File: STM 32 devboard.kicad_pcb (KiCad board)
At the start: 2 copper layers, 20 x 50 mm, 29 parts, among them J1 Conn_01x10_Pin, J2 Conn_01x10_Pin, J3 USB_B_Micro, SW1 SW_SPDT, U1 AMS1117-3.3, U2 STM32F103C8T6, Y1 16MHz

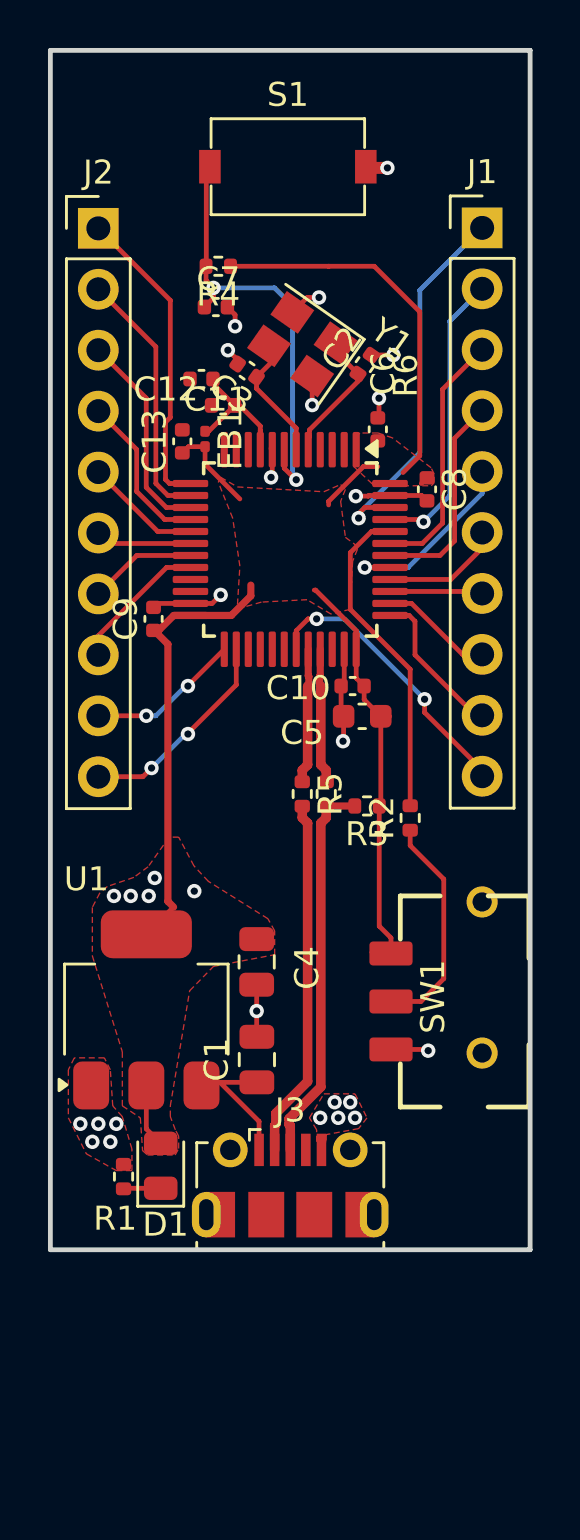
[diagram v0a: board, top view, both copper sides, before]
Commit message: Added USB-C port.
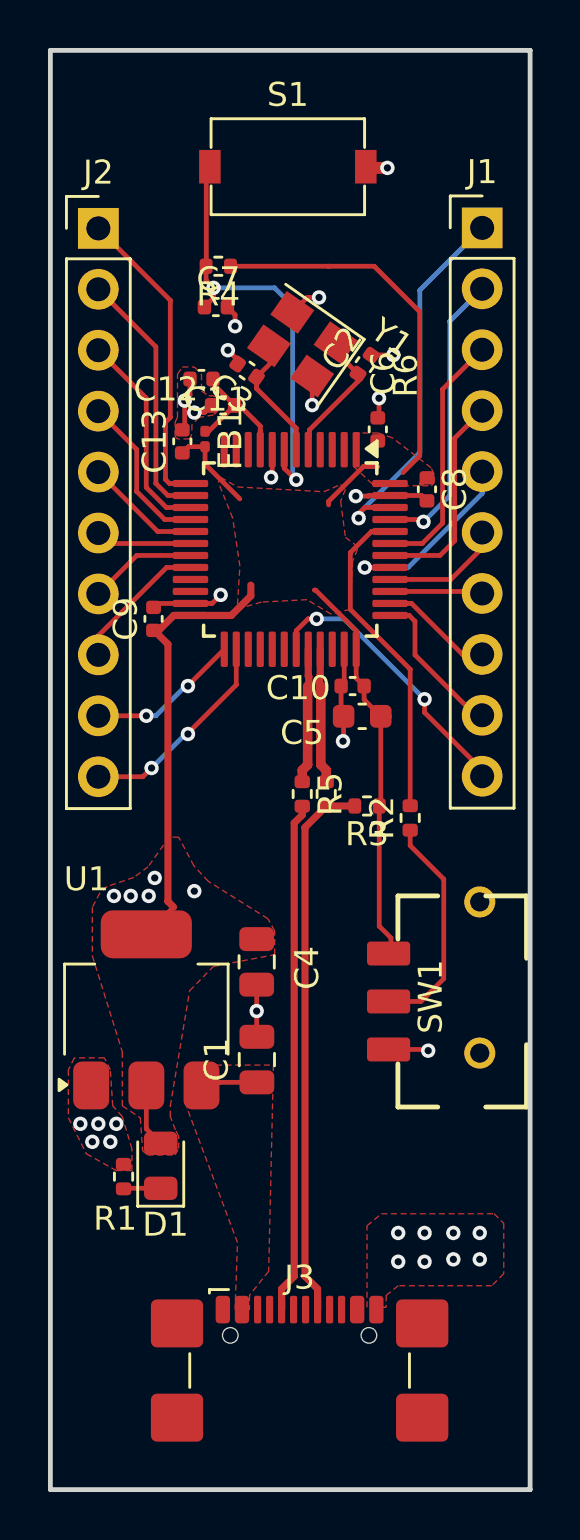
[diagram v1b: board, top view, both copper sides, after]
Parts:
- C1: value 22uF -> 22u
- C10, C6, C8, C9: value 100nF -> 100n
- C11: value 10nF -> 10n
- C12, C13: value 1uF -> 1u
- C2, C3: value 12pF -> 12p
- C5: value 10uF -> 10u
- J3: value USB_B_Micro -> USB_C_Receptacle; footprint Connector_USB:USB_Micro-B_Molex-105017-0001 -> Connector_USB:USB_C_Receptacle_GCT_USB4110
- moved J3 8.88 mm to (22.4, 68.2)
- moved SW1 0.10 mm to (27.4, 51.6)
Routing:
- net /USB_D+: track 16.2 -> 22.8 mm
- net /USB_D-: track 15.0 -> 21.3 mm
- net VBUS: track 6.50 -> 3.01 mm
- net GND: track 23.4 -> 25.9 mm, vias 23 -> 28
- added copper zone on F.Cu, net VBUS
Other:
- board size 20 x 50 mm -> 20 x 60 mm
